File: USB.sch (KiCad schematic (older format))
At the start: 4 parts, among them J2 USB_C_Receptacle_USB2.0

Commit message: Routing angefangen
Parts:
- added C6, C7, C8, C9: 10µ, Capacitor_SMD:C_1206_3216Metric_Pad1.33x1.80mm_HandSolder, symbol Device:C_Small
- added D54: LED_Small, LED_SMD:LED_0603_1608Metric_Pad1.05x0.95mm_HandSolder, symbol Device:LED_Small
- added J3: Conn_01x02_Male, Connector_JST:JST_PH_S2B-PH-K_1x02_P2.00mm_Horizontal, symbol Connector:Conn_01x02_Male
- added R10: 470, Resistor_SMD:R_0603_1608Metric_Pad0.98x0.95mm_HandSolder, symbol Device:R_Small
- added R9: 2k2, Resistor_SMD:R_0603_1608Metric_Pad0.98x0.95mm_HandSolder, symbol Device:R_Small
- added U5: MCP73831-2-OT, Package_TO_SOT_SMD:SOT-23-5, symbol Battery_Management:MCP73831-2-OT
- added U6: AMS1117-3.3, Package_TO_SOT_SMD:SOT-223-3_TabPin2, symbol Regulator_Linear:AMS1117-3.3
- J2: footprint Connector_USB:USB_C_Receptacle_Amphenol_12401548E4-2A_CircularHoles -> msp430_Keyboard:632723300011
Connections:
- net GND: now also C6.2, C7.2, C8.2, C9.2, J3.2 (Pin_2), R9.1, U5.2 (VSS), U6.1 (GND)
- net VBUS: now also C6.1, D54.2 (A), U5.4 (VDD)
- new net: R10.1, U5.1 (STAT)
- new net: R9.2, U5.5 (PROG)
- new net: D54.1 (K), R10.2
- new net +3V3: C9.1, U6.2 (VO)
- new net +BATT: C7.1, C8.1, J3.1 (Pin_1), U5.3 (VBAT), U6.3 (VI)

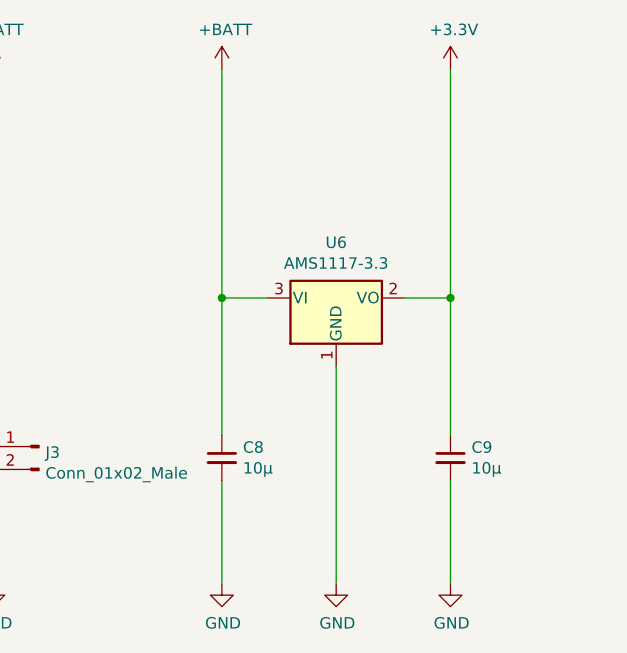
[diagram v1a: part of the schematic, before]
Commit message: Layout sent to JLCPCB
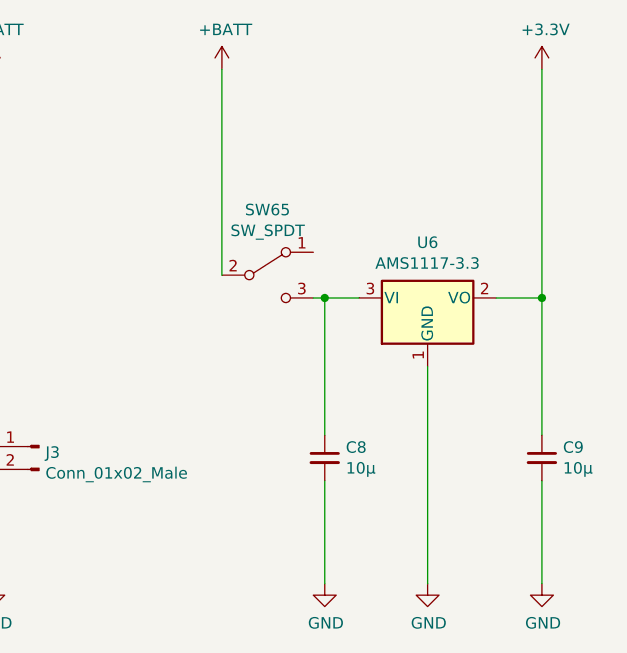
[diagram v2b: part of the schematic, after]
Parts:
- added SW65: SW_SPDT, HS-Wismar:APEM_SLG12014, symbol Switch:SW_SPDT
- R6, R7, R8: footprint Resistor_SMD:R_0603_1608Metric -> Resistor_SMD:R_0603_1608Metric_Pad0.98x0.95mm_HandSolder
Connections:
- net +BATT: now also SW65.2 (B); no longer C8.1, U6.3 (VI)
- new net: C8.1, SW65.3 (C), U6.3 (VI)
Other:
- moved on the sheet: C8, C9, U6
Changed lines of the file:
@@
 F 0 "R7" H 3859 3796 50  0000 L CNN
 F 1 "5k1" H 3859 3705 50  0000 L CNN
-F 2 "Resistor_SMD:R_0603_1608Metric" H 3800 3750 50  0001 C CNN
+F 2 "Resistor_SMD:R_0603_1608Metric_Pad0.98x0.95mm_HandSolder" H 3800 3750 50  0001 C CNN
 F 3 "~" H 3800 3750 50  0001 C CNN
 	1    3800 3750
@@
 F 0 "R8" H 4009 3796 50  0000 L CNN
 F 1 "5k1" H 4009 3705 50  0000 L CNN
-F 2 "Resistor_SMD:R_0603_1608Metric" H 3950 3750 50  0001 C CNN
+F 2 "Resistor_SMD:R_0603_1608Metric_Pad0.98x0.95mm_HandSolder" H 3950 3750 50  0001 C CNN
 F 3 "~" H 3950 3750 50  0001 C CNN
 	1    3950 3750
@@
 F 0 "R6" H 2659 3996 50  0000 L CNN
 F 1 "1Meg" H 2659 3905 50  0000 L CNN
-F 2 "Resistor_SMD:R_0603_1608Metric" H 2600 3950 50  0001 C CNN
+F 2 "Resistor_SMD:R_0603_1608Metric_Pad0.98x0.95mm_HandSolder" H 2600 3950 50  0001 C CNN
 F 3 "~" H 2600 3950 50  0001 C CNN
 	1    2600 3950
@@
 L Regulator_Linear:AMS1117-3.3 U6
 U 1 1 60FC7E0F
-P 8750 2950
-F 0 "U6" H 8750 3192 50  0000 C CNN
-F 1 "AMS1117-3.3" H 8750 3101 50  0000 C CNN
-F 2 "Package_TO_SOT_SMD:SOT-223-3_TabPin2" H 8750 3150 50  0001 C CNN
-F 3 "http://www.advanced-monolithic.com/pdf/ds1117.pdf" H 8850 2700 50  0001 C CNN
-	1    8750 2950
+P 9150 2950
+F 0 "U6" H 9150 3192 50  0000 C CNN
+F 1 "AMS1117-3.3" H 9150 3101 50  0000 C CNN
+F 2 "Package_TO_SOT_SMD:SOT-223-3_TabPin2" H 9150 3150 50  0001 C CNN
+F 3 "http://www.advanced-monolithic.com/pdf/ds1117.pdf" H 9250 2700 50  0001 C CNN
+	1    9150 2950
 	1    0    0    -1
 $EndComp
@@
 L Device:C_Small C8
 U 1 1 60FCA10F
-P 8250 3650
-F 0 "C8" H 8342 3696 50  0000 L CNN
-F 1 "10µ" H 8342 3605 50  0000 L CNN
-F 2 "Capacitor_SMD:C_1206_3216Metric_Pad1.33x1.80mm_HandSolder" H 8250 3650 50  0001 C CNN
-F 3 "~" H 8250 3650 50  0001 C CNN
-	1    8250 3650
+P 8700 3650
+F 0 "C8" H 8792 3696 50  0000 L CNN
+F 1 "10µ" H 8792 3605 50  0000 L CNN
+F 2 "Capacitor_SMD:C_1206_3216Metric_Pad1.33x1.80mm_HandSolder" H 8700 3650 50  0001 C CNN
+F 3 "~" H 8700 3650 50  0001 C CNN
+	1    8700 3650
 	1    0    0    -1
 $EndComp
@@
 L Device:C_Small C9
 U 1 1 60FCAB70
-P 9250 3650
-F 0 "C9" H 9342 3696 50  0000 L CNN
-F 1 "10µ" H 9342 3605 50  0000 L CNN
-F 2 "Capacitor_SMD:C_1206_3216Metric_Pad1.33x1.80mm_HandSolder" H 9250 3650 50  0001 C CNN
-F 3 "~" H 9250 3650 50  0001 C CNN
-	1    9250 3650
-	1    0    0    -1
-$EndComp
-Wire Wire Line
-	8250 3550 8250 2950
-Wire Wire Line
-	8250 2950 8450 2950
-Wire Wire Line
-	9050 2950 9250 2950
-Wire Wire Line
-	9250 2950 9250 3550
+P 9650 3650
+F 0 "C9" H 9742 3696 50  0000 L CNN
+F 1 "10µ" H 9742 3605 50  0000 L CNN
+F 2 "Capacitor_SMD:C_1206_3216Metric_Pad1.33x1.80mm_HandSolder" H 9650 3650 50  0001 C CNN
+F 3 "~" H 9650 3650 50  0001 C CNN
+	1    9650 3650
+	1    0    0    -1
+$EndComp
+Wire Wire Line
+	8650 2950 8700 2950
+Wire Wire Line
+	9450 2950 9650 2950
+Wire Wire Line
+	9650 2950 9650 3550
 $Comp
 L power:GND #PWR020
 U 1 1 60FCCF5B
-P 8250 4200
-F 0 "#PWR020" H 8250 3950 50  0001 C CNN
-F 1 "GND" H 8255 4027 50  0000 C CNN
-F 2 "" H 8250 4200 50  0001 C CNN
-F 3 "" H 8250 4200 50  0001 C CNN
-	1    8250 4200
+P 8700 4200
+F 0 "#PWR020" H 8700 3950 50  0001 C CNN
+F 1 "GND" H 8705 4027 50  0000 C CNN
+F 2 "" H 8700 4200 50  0001 C CNN
+F 3 "" H 8700 4200 50  0001 C CNN
+	1    8700 4200
 	1    0    0    -1
 $EndComp
@@
 L power:GND #PWR021
 U 1 1 60FCD507
-P 8750 4200
-F 0 "#PWR021" H 8750 3950 50  0001 C CNN
-F 1 "GND" H 8755 4027 50  0000 C CNN
-F 2 "" H 8750 4200 50  0001 C CNN
-F 3 "" H 8750 4200 50  0001 C CNN
-	1    8750 4200
+P 9150 4200
+F 0 "#PWR021" H 9150 3950 50  0001 C CNN
+F 1 "GND" H 9155 4027 50  0000 C CNN
+F 2 "" H 9150 4200 50  0001 C CNN
+F 3 "" H 9150 4200 50  0001 C CNN
+	1    9150 4200
 	1    0    0    -1
 $EndComp
@@
 L power:GND #PWR023
 U 1 1 60FCD983
-P 9250 4200
-F 0 "#PWR023" H 9250 3950 50  0001 C CNN
-F 1 "GND" H 9255 4027 50  0000 C CNN
-F 2 "" H 9250 4200 50  0001 C CNN
-F 3 "" H 9250 4200 50  0001 C CNN
-	1    9250 4200
-	1    0    0    -1
-$EndComp
-Wire Wire Line
-	9250 4200 9250 3750
-Wire Wire Line
-	8750 3250 8750 4200
-Wire Wire Line
-	8250 3750 8250 4200
+P 9650 4200
+F 0 "#PWR023" H 9650 3950 50  0001 C CNN
+F 1 "GND" H 9655 4027 50  0000 C CNN
+F 2 "" H 9650 4200 50  0001 C CNN
+F 3 "" H 9650 4200 50  0001 C CNN
+	1    9650 4200
+	1    0    0    -1
+$EndComp
+Wire Wire Line
+	9650 4200 9650 3750
+Wire Wire Line
+	9150 3250 9150 4200
+Wire Wire Line
+	8700 3750 8700 4200
 $Comp
 L power:+BATT #PWR019
@@
 	1    0    0    -1
 $EndComp
-Wire Wire Line
-	8250 1950 8250 2950
-Connection ~ 8250 2950
 $Comp
 L power:+3.3V #PWR022
 U 1 1 60FD09AE
-P 9250 1950
-F 0 "#PWR022" H 9250 1800 50  0001 C CNN
-F 1 "+3.3V" H 9265 2123 50  0000 C CNN
-F 2 "" H 9250 1950 50  0001 C CNN
-F 3 "" H 9250 1950 50  0001 C CNN
-	1    9250 1950
-	1    0    0    -1
-$EndComp
-Wire Wire Line
-	9250 1950 9250 2950
-Connection ~ 9250 2950
+P 9650 1950
+F 0 "#PWR022" H 9650 1800 50  0001 C CNN
+F 1 "+3.3V" H 9665 2123 50  0000 C CNN
+F 2 "" H 9650 1950 50  0001 C CNN
+F 3 "" H 9650 1950 50  0001 C CNN
+	1    9650 1950
+	1    0    0    -1
+$EndComp
+Wire Wire Line
+	9650 1950 9650 2950
+Connection ~ 9650 2950
+Wire Wire Line
+	8250 1950 8250 2850
+$Comp
+L Switch:SW_SPDT SW65
+U 1 1 60FF63D1
+P 8450 2850
+F 0 "SW65" H 8450 3135 50  0000 C CNN
+F 1 "SW_SPDT" H 8450 3044 50  0000 C CNN
+F 2 "HS-Wismar:APEM_SLG12014" H 8450 2850 50  0001 C CNN
+F 3 "~" H 8450 2850 50  0001 C CNN
+	1    8450 2850
+	1    0    0    -1
+$EndComp
+Wire Wire Line
+	8700 3550 8700 2950
+Connection ~ 8700 2950
+Wire Wire Line
+	8700 2950 8850 2950
 $EndSCHEMATC

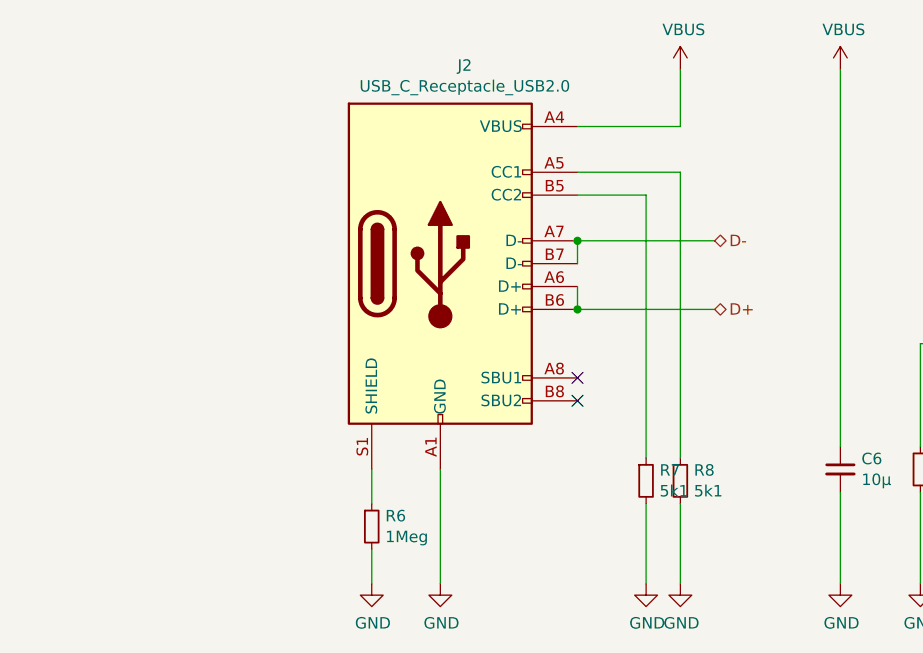
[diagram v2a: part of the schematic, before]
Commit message: Filterung in den USB-Leitungen, VBus besser abgeblockt, Enter Taste gedreht
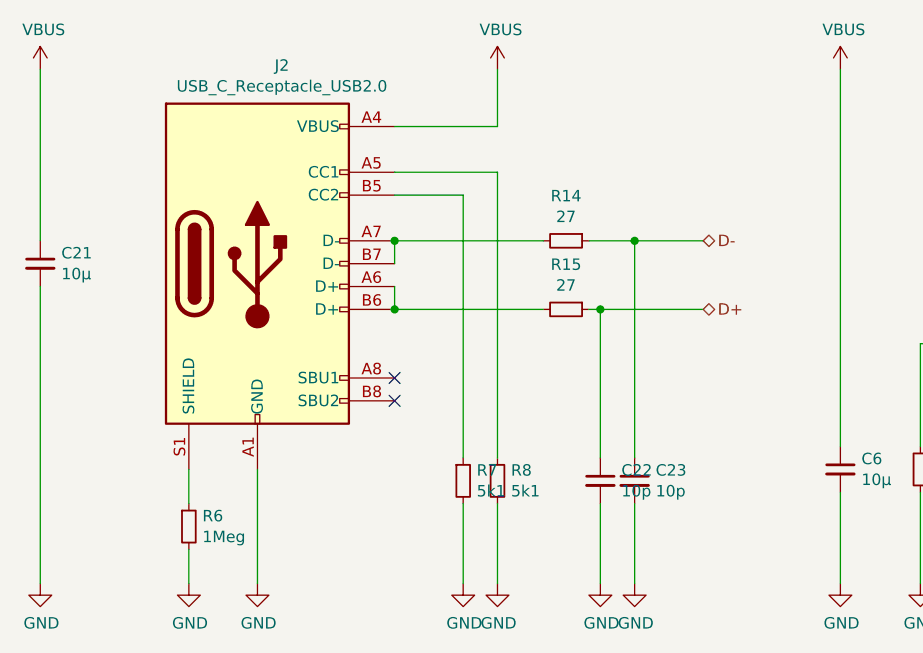
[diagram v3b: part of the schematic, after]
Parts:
- added C21: 10μ, Capacitor_SMD:C_1206_3216Metric_Pad1.33x1.80mm_HandSolder, symbol Device:C_Small
- added C22, C23: 10p, Capacitor_SMD:C_0603_1608Metric_Pad1.08x0.95mm_HandSolder, symbol Device:C_Small
- added R14, R15: 27, Resistor_SMD:R_0603_1608Metric_Pad0.98x0.95mm_HandSolder, symbol Device:R_Small
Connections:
- net D+: now also C22.1, R15.1; no longer J2.A6 (D+), J2.B6 (D+)
- net D-: now also C23.1, R14.1; no longer J2.A7 (D-), J2.B7 (D-)
- net GND: now also C21.2, C22.2, C23.2
- net VBUS: now also C21.1
- new net: J2.A6 (D+), J2.B6 (D+), R15.2
- new net: J2.A7 (D-), J2.B7 (D-), R14.2
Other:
- moved on the sheet: J2, R6, R7, R8
